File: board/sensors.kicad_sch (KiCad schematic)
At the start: 59 parts, among them J2 SWIM, U6 STM8S003F3P, U7 MAX-M8C, U8 LM324, U9 LM324

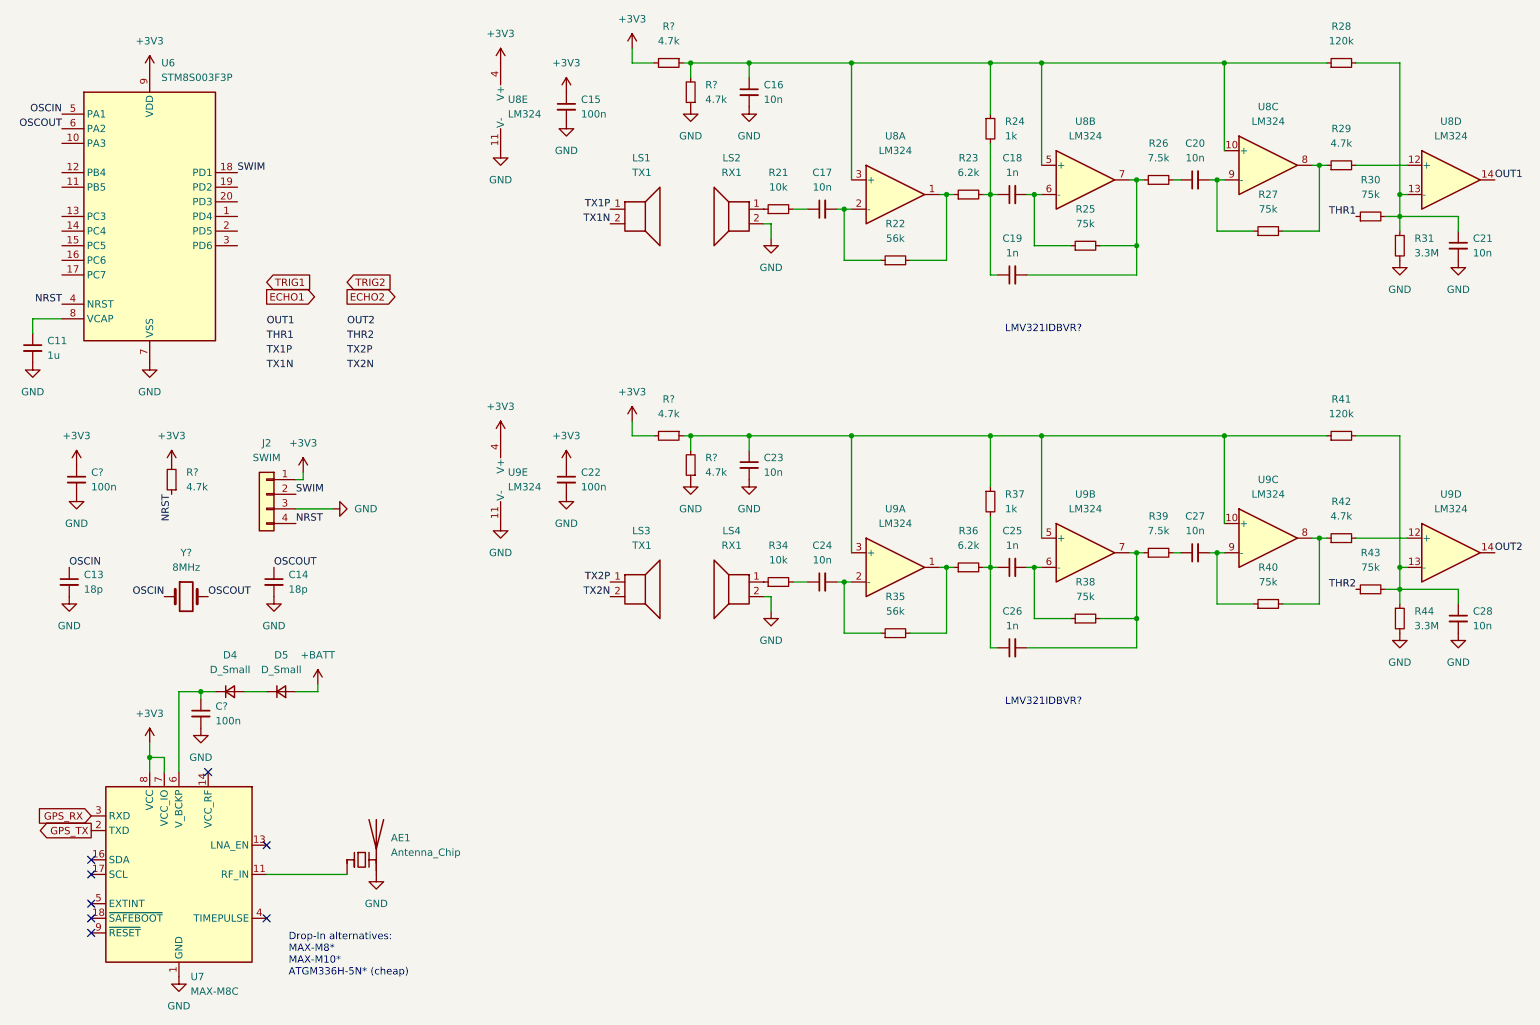
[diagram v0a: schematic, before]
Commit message: New power management IC, some cleanup
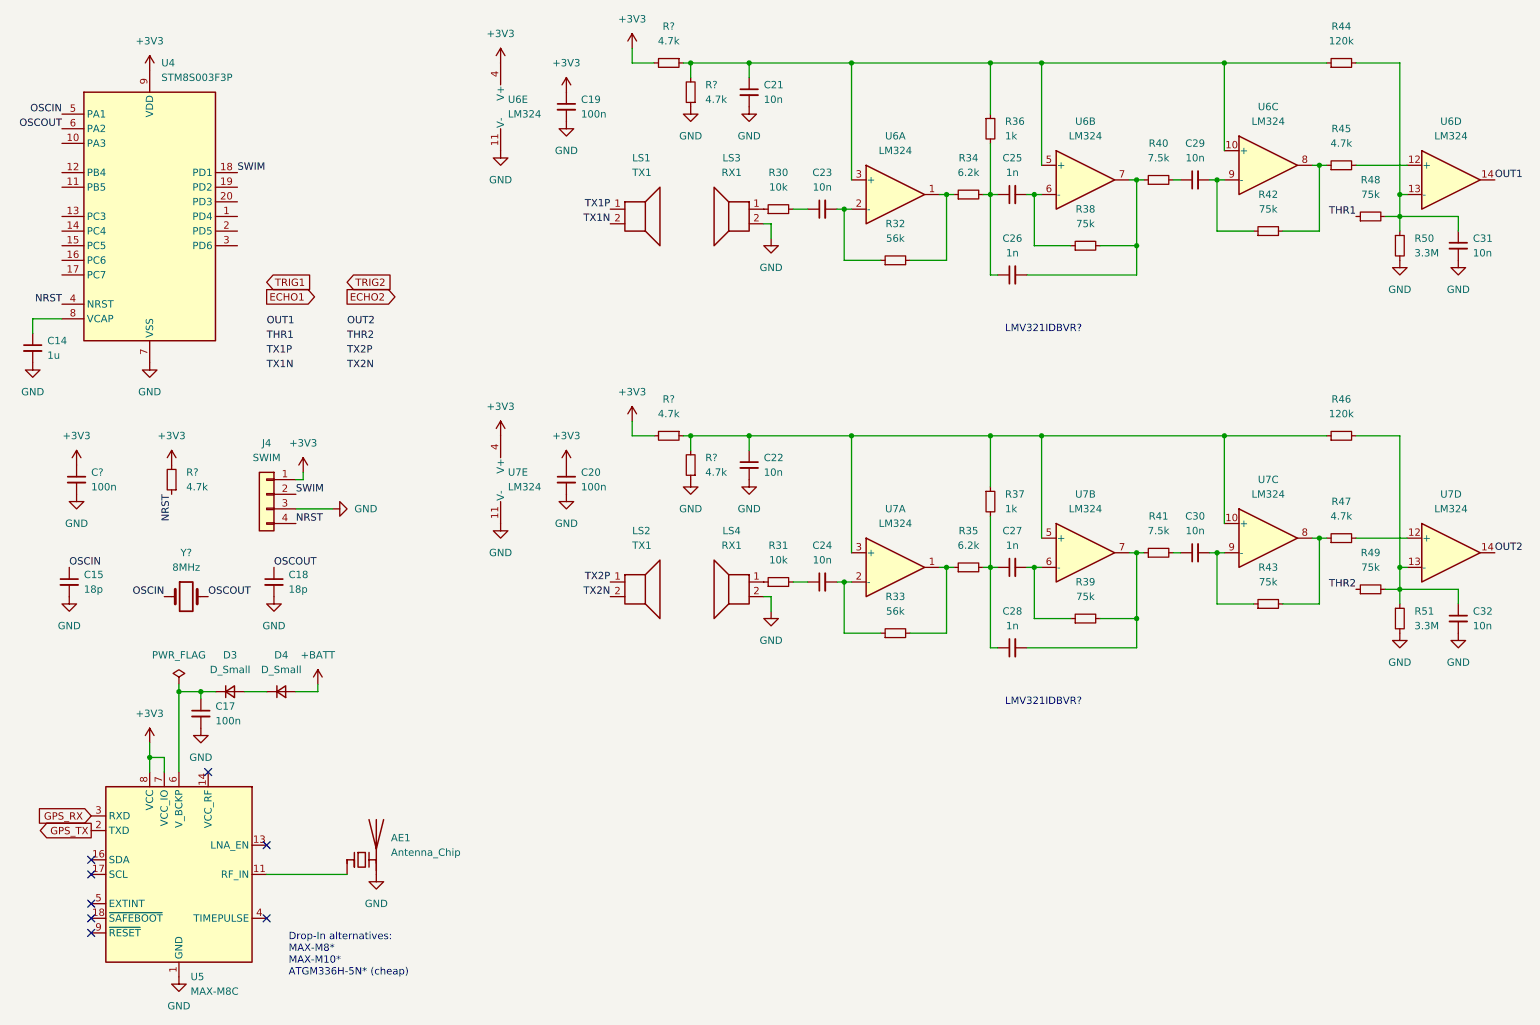
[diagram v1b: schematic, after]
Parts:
- gave numbers to parts that had none: 1
- renumbered C11 to C14, C13 to C15, C14 to C18, C15 to C19, C22 to C20, C16 to C21, C23 to C22, C17 to C23, C18 to C25, C19 to C26, C25 to C27, C26 to C28, C20 to C29, C27 to C30, C21 to C31, C28 to C32, D4 to D3, D5 to D4, J2 to J4, LS3 to LS2, LS2 to LS3, R21 to R30, R34 to R31, R22 to R32, R35 to R33, R23 to R34, R36 to R35, R24 to R36, R25 to R38, R38 to R39, R26 to R40, R39 to R41, R27 to R42, R40 to R43, R28 to R44, R29 to R45, R41 to R46, R42 to R47, R30 to R48, R43 to R49, R31 to R50, R44 to R51, U6 to U4, U7 to U5, U8 to U6, U9 to U7

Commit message: Add kibot/kicost config and sample cost entry for antenna chip
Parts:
- AE1: kicost:JLC:pricing (none) -> 1:USD1.0297; 10:USD0.9651; 100:USD0.5724; 1000:USD0.6065
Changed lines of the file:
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@@
+      (effects (font (size 1.27 1.27)) hide)
+    )
+    (property "kicost:JLC:pricing" "1:USD1.0297; 10:USD0.9651; 100:USD0.5724; 1000:USD0.6065" (id 13) (at 76.2 168.91 0)
       (effects (font (size 1.27 1.27)) hide)
     )

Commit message: Add kibot:JLC:pricing from existing columns
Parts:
- AE1: kicost:JLC:pricing 1:USD1.0297; 10:USD0.9651; 100:USD0.5724; 1000:USD0.6065 -> 1: USD 1.0297; 10: USD 0.8651; 100: USD 0.5724; 1000: USD0.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
- C14: kicost:JLC:pricing (none) -> 1: USD 0.056; 10: USD 0.0056; 100: USD 0.0028; 1000: USD0.0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
- C17, C19, C20, C?: kicost:JLC:pricing (none) -> 1: USD 0.042; 10: USD 0.0042; 100: USD 0.0021; 1000: USD0.0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
- J4: kicost:JLC:pricing (none) -> 1: USD 0.1105; 10: USD 0.0442; 100: USD 0.0179; 1000: USD0.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
- LS1, LS2, LS3, LS4: kicost:JLC:pricing (none) -> 1: USD 1.5383; 10: USD 1.2985; 100: USD 1.1671; 1000: USD1.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
- U4: kicost:JLC:pricing (none) -> 1: USD 0.7209; 10: USD 0.7084; 100: USD 0.7084; 1000: USD0.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
- U5: kicost:JLC:pricing (none) -> 1: USD 21; 10: USD 15.73; 100: USD 10.32; 1000: USD10.32
- U6, U7: kicost:JLC:pricing (none) -> 1: USD 0.1235; 10: USD 0.0971; 100: USD 0.0728; 1000: USD0.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
- Y?: kicost:JLC:pricing (none) -> 1: USD 0.164; 10: USD 0.082; 100: USD 0.0576; 1000: USD0.04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
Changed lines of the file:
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@@
+      (effects (font (size 1.27 1.27)) hide)
+    )
+    (property "kicost:JLC:pricing" "1: USD 0.042; 10: USD 0.0042; 100: USD 0.0021; 1000: USD0.0014" (id 16) (at 26.67 102.87 0)
       (effects (font (size 1.27 1.27)) hide)
     )
@@
       (effects (font (size 1.27 1.27)) hide)
     )
-    (property "kicost:JLC:pricing" "1:USD1.0297; 10:USD0.9651; 100:USD0.5724; 1000:USD0.6065" (id 13) (at 76.2 168.91 0)
+    (property "kicost:JLC:pricing" "1: USD 1.0297; 10: USD 0.8651; 100: USD 0.5724; 1000: USD0.6065" (id 13) (at 76.2 168.91 0)
       (effects (font (size 1.27 1.27)) hide)
     )
@@
       (effects (font (size 1.27 1.27)) hide)
     )
+    (property "kicost:JLC:pricing" "1: USD 1.5383; 10: USD 1.2985; 100: USD 1.1671; 1000: USD1.0179" (id 13) (at 124.46 55.88 0)
+      (effects (font (size 1.27 1.27)) hide)
+    )
     (pin "1")
     (pin "2")
@@
     )
     (property "PCBA" "no" (id 11) (at 44.45 171.45 0)
+      (effects (font (size 1.27 1.27)) hide)
+    )
+    (property "kicost:JLC:pricing" "1: USD 21; 10: USD 15.73; 100: USD 10.32; 1000: USD10.32" (id 12) (at 44.45 171.45 0)
       (effects (font (size 1.27 1.27)) hide)
     )
@@
       (effects (font (size 1.27 1.27)) hide)
     )
+    (property "kicost:JLC:pricing" "1: USD 1.5383; 10: USD 1.2985; 100: USD 1.1671; 1000: USD1.0179" (id 13) (at 140.97 55.88 0)
+      (effects (font (size 1.27 1.27)) hide)
+    )
     (pin "1")
     (pin "2")
@@
     )
     (property "PCBA" "yes" (id 12) (at 265.43 50.8 0)
+      (effects (font (size 1.27 1.27)) hide)
+    )
+    (property "kicost:JLC:pricing" "1: USD 0.1235; 10: USD 0.0971; 100: USD 0.0728; 1000: USD0.0696" (id 13) (at 265.43 50.8 0)
       (effects (font (size 1.27 1.27)) hide)
     )
@@
       (effects (font (size 1.27 1.27)) hide)
     )
+    (property "kicost:JLC:pricing" "1: USD 0.1235; 10: USD 0.0971; 100: USD 0.0728; 1000: USD0.0696" (id 13) (at 102.87 38.1 0)
+      (effects (font (size 1.27 1.27)) hide)
+    )
     (pin "1")
     (pin "2")
@@
       (effects (font (size 1.27 1.27)) hide)
     )
+    (property "kicost:JLC:pricing" "1: USD 0.042; 10: USD 0.0042; 100: USD 0.0021; 1000: USD0.0014" (id 13) (at 111.76 38.1 0)
+      (effects (font (size 1.27 1.27)) hide)
+    )
     (pin "1")
     (pin "2")
@@
     )
     (property "PCBA" "yes" (id 12) (at 102.87 102.87 0)
+      (effects (font (size 1.27 1.27)) hide)
+    )
+    (property "kicost:JLC:pricing" "1: USD 0.1235; 10: USD 0.0971; 100: USD 0.0728; 1000: USD0.0696" (id 13) (at 102.87 102.87 0)
       (effects (font (size 1.27 1.27)) hide)
     )
@@
       (effects (font (size 1.27 1.27)) hide)
     )
+    (property "kicost:JLC:pricing" "1: USD 0.056; 10: USD 0.0056; 100: USD 0.0028; 1000: USD0.0027" (id 13) (at 19.05 80.01 0)
+      (effects (font (size 1.27 1.27)) hide)
+    )
     (pin "1")
     (pin "2")
@@
     )
     (property "PCBA" "yes" (id 12) (at 233.68 113.03 0)
+      (effects (font (size 1.27 1.27)) hide)
+    )
+    (property "kicost:JLC:pricing" "1: USD 0.1235; 10: USD 0.0971; 100: USD 0.0728; 1000: USD0.0696" (id 13) (at 233.68 113.03 0)
       (effects (font (size 1.27 1.27)) hide)
     )
@@
       (effects (font (size 1.27 1.27)) hide)
     )
+    (property "kicost:JLC:pricing" "1: USD 1.5383; 10: USD 1.2985; 100: USD 1.1671; 1000: USD1.0179" (id 13) (at 140.97 120.65 0)
+      (effects (font (size 1.27 1.27)) hide)
+    )
     (pin "1")
     (pin "2")
@@
     )
     (property "PCBA" "yes" (id 12) (at 201.93 50.8 0)
+      (effects (font (size 1.27 1.27)) hide)
+    )
+    (property "kicost:JLC:pricing" "1: USD 0.1235; 10: USD 0.0971; 100: USD 0.0728; 1000: USD0.0696" (id 13) (at 201.93 50.8 0)
       (effects (font (size 1.27 1.27)) hide)
     )
@@
       (effects (font (size 1.27 1.27)) hide)
     )
+    (property "kicost:JLC:pricing" "1: USD 0.042; 10: USD 0.0042; 100: USD 0.0021; 1000: USD0.0014" (id 13) (at 48.26 143.51 0)
+      (effects (font (size 1.27 1.27)) hide)
+    )
     (pin "1")
     (pin "2")
@@
       (effects (font (size 1.27 1.27)) hide)
     )
+    (property "kicost:JLC:pricing" "1: USD 0.042; 10: USD 0.0042; 100: USD 0.0021; 1000: USD0.0014" (id 13) (at 111.76 102.87 0)
+      (effects (font (size 1.27 1.27)) hide)
+    )
     (pin "1")
     (pin "2")
@@
     )
     (property "PCBA" "yes" (id 12) (at 233.68 48.26 0)
+      (effects (font (size 1.27 1.27)) hide)
+    )
+    (property "kicost:JLC:pricing" "1: USD 0.1235; 10: USD 0.0971; 100: USD 0.0728; 1000: USD0.0696" (id 13) (at 233.68 48.26 0)
       (effects (font (size 1.27 1.27)) hide)
     )
@@
       (effects (font (size 1.27 1.27)) hide)
     )
+    (property "kicost:JLC:pricing" "1: USD 0.1105; 10: USD 0.0442; 100: USD 0.0179; 1000: USD0.0142" (id 13) (at 59.69 105.41 0)
+      (effects (font (size 1.27 1.27)) hide)
+    )
     (pin "1")
     (pin "2")
@@
     )
     (property "PCBA" "yes" (id 12) (at 39.37 57.15 0)
+      (effects (font (size 1.27 1.27)) hide)
+    )
+    (property "kicost:JLC:pricing" "1: USD 0.7209; 10: USD 0.7084; 100: USD 0.7084; 1000: USD0.7084" (id 13) (at 39.37 57.15 0)
       (effects (font (size 1.27 1.27)) hide)
     )
@@
     )
     (property "PCBA" "yes" (id 12) (at 168.91 118.11 0)
+      (effects (font (size 1.27 1.27)) hide)
+    )
+    (property "kicost:JLC:pricing" "1: USD 0.1235; 10: USD 0.0971; 100: USD 0.0728; 1000: USD0.0696" (id 13) (at 168.91 118.11 0)
       (effects (font (size 1.27 1.27)) hide)
     )
@@
       (effects (font (size 1.27 1.27)) hide)
     )
+    (property "kicost:JLC:pricing" "1: USD 0.1235; 10: USD 0.0971; 100: USD 0.0728; 1000: USD0.0696" (id 13) (at 201.93 115.57 0)
+      (effects (font (size 1.27 1.27)) hide)
+    )
     (pin "1")
     (pin "2")
@@
       (effects (font (size 1.27 1.27)) hide)
     )
+    (property "kicost:JLC:pricing" "1: USD 0.1235; 10: USD 0.0971; 100: USD 0.0728; 1000: USD0.0696" (id 13) (at 265.43 115.57 0)
+      (effects (font (size 1.27 1.27)) hide)
+    )
     (pin "1")
     (pin "2")
@@
       (effects (font (size 1.27 1.27)) hide)
     )
+    (property "kicost:JLC:pricing" "1: USD 0.1235; 10: USD 0.0971; 100: USD 0.0728; 1000: USD0.0696" (id 13) (at 168.91 53.34 0)
+      (effects (font (size 1.27 1.27)) hide)
+    )
     (pin "1")
     (pin "2")
@@
       (effects (font (size 1.27 1.27)) hide)
     )
+    (property "kicost:JLC:pricing" "1: USD 1.5383; 10: USD 1.2985; 100: USD 1.1671; 1000: USD1.0179" (id 13) (at 124.46 120.65 0)
+      (effects (font (size 1.27 1.27)) hide)
+    )
     (pin "1")
     (pin "2")
@@
       (effects (font (size 1.27 1.27)) hide)
     )
+    (property "kicost:JLC:pricing" "1: USD 0.164; 10: USD 0.082; 100: USD 0.0576; 1000: USD0.0464" (id 16) (at 45.72 123.19 0)
+      (effects (font (size 1.27 1.27)) hide)
+    )

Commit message: Add more footprints, prices and part numbers
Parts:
- C14: footprint (none) -> Capacitor_SMD:C_0603_1608Metric; kicost:JLC:pricing 1: USD 0.056; 10: USD 0.0056; 100: USD 0.0028; 1000: USD0.0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 -> 1: USD 0.056; 10: USD 0.0056; 100: USD 0.0028; 1000: USD 0.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
- C15, C18: footprint (none) -> Capacitor_SMD:C_0603_1608Metric; JLC_BasicPart (none) -> yes; JLC_PN (none) -> C1647; MPN (none) -> CL10C180JB8NNNC; Manufacturer (none) -> Samsung Electro-Mechanics; kicost:JLC:pricing (none) -> 1: USD 0.0069; 200: USD 0.0058; 800: USD 0.0051; 1600: USD 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
- C17, C19, C20, C?: footprint (none) -> Capacitor_SMD:C_0603_1608Metric; kicost:JLC:pricing 1: USD 0.042; 10: USD 0.0042; 100: USD 0.0021; 1000: USD0.0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 -> 1: USD 0.0020; 200: USD 0.0016; 800: USD 0.0013; 1600: USD 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
- C21, C22, C23, C24, C29, C30, C31, C32: footprint (none) -> Capacitor_SMD:C_0603_1608Metric; JLC_BasicPart (none) -> yes; JLC_PN (none) -> C57112; MPN (none) -> 0603B103K500NT; Manufacturer (none) -> FH (Guangdong Fenghua Advanced Tech); kicost:JLC:pricing (none) -> 1: USD 0.0012
- C25, C26, C27, C28: footprint (none) -> Capacitor_SMD:C_0603_1608Metric; JLC_BasicPart (none) -> yes; JLC_PN (none) -> C1588; MPN (none) -> CL10B102KB8NNNC; Manufacturer (none) -> Samsung Electro-Mechanics; kicost:JLC:pricing (none) -> 1: USD 0.0026; 200: USD 0.0020; 800: USD 0.0017; 1600: USD 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
- D3, D4: footprint (none) -> Diode_SMD:D_SMA; JLC_BasicPart (none) -> yes; JLC_PN (none) -> C2480; MPN (none) -> SS14; Manufacturer (none) -> MDD（Microdiode Electronics）; kicost:JLC:pricing (none) -> 1: USD 0.0137; 50: USD 0.0111; 150: USD 0.0097; 500: USD 0.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
- J4: kicost:JLC:pricing 1: USD 0.1105; 10: USD 0.0442; 100: USD 0.0179; 1000: USD0.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 -> 1: USD 0.1105; 10: USD 0.0442; 100: USD 0.0179; 1000: USD 0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
- LS1, LS2, LS3, LS4: kicost:JLC:pricing 1: USD 1.5383; 10: USD 1.2985; 100: USD 1.1671; 1000: USD1.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 -> 1: USD 1.5383; 10: USD 1.2985; 100: USD 1.1671; 1000: USD 1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
- R30, R31: footprint (none) -> Resistor_SMD:R_0603_1608Metric; JLC_BasicPart (none) -> yes; JLC_PN (none) -> C25197; MPN (none) -> 0603WAF510KT5E; Manufacturer (none) -> UNI-ROYAL(Uniroyal Elec); kicost:JLC:pricing (none) -> 1: USD 0.0014; 200: USD 0.0011; 1000: USD 0.0009; 2000: USD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
- R32, R33: footprint (none) -> Resistor_SMD:R_0603_1608Metric; JLC_BasicPart (none) -> yes; JLC_PN (none) -> C23206; MPN (none) -> 0603WAF5602T5E; Manufacturer (none) -> UNI-ROYAL(Uniroyal Elec); kicost:JLC:pricing (none) -> 1: USD 0.0009; 200: USD 0.0007; 1000: USD 0.0006; 2000: USD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
- R34, R35: footprint (none) -> Resistor_SMD:R_0603_1608Metric; JLC_BasicPart (none) -> yes; JLC_PN (none) -> C4260; MPN (none) -> 0603WAF6201T5E; Manufacturer (none) -> UNI-ROYAL(Uniroyal Elec); kicost:JLC:pricing (none) -> 1: USD 0.0009; 200: USD 0.0007; 1000: USD 0.0006; 10000: US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
- R36, R37: footprint (none) -> Resistor_SMD:R_0603_1608Metric; JLC_BasicPart (none) -> yes; JLC_PN (none) -> C21190; MPN (none) -> 0603WAF1001T5E; Manufacturer (none) -> UNI-ROYAL(Uniroyal Elec); kicost:JLC:pricing (none) -> 1: USD 0.0005; 200: USD 0.0004
- R38, R39, R42, R43, R48, R49: footprint (none) -> Resistor_SMD:R_0603_1608Metric; JLC_BasicPart (none) -> yes; JLC_PN (none) -> C23242; MPN (none) -> 0603WAF7502T5E; Manufacturer (none) -> UNI-ROYAL(Uniroyal Elec); kicost:JLC:pricing (none) -> 1: USD 0.0010; 200: USD 0.0007; 1000: USD 0.0006; 10000: US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
- R40, R41: footprint (none) -> Resistor_SMD:R_0603_1608Metric; JLC_BasicPart (none) -> yes; JLC_PN (none) -> C23234; MPN (none) -> 0603WAF7501T5E; Manufacturer (none) -> UNI-ROYAL(Uniroyal Elec); kicost:JLC:pricing (none) -> 1: USD 0.0009; 200: USD 0.0007; 1000: USD 0.0006; 10000: US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
- R44, R46: footprint (none) -> Resistor_SMD:R_0603_1608Metric; JLC_BasicPart (none) -> yes; JLC_PN (none) -> C25808; MPN (none) -> 0603WAF1203T5E; Manufacturer (none) -> UNI-ROYAL(Uniroyal Elec); kicost:JLC:pricing (none) -> 1: USD 0.0010; 200: USD 0.0007; 1000: USD 0.0006; 10000: US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
- R45, R47, R? (x5): footprint (none) -> Resistor_SMD:R_0603_1608Metric; JLC_BasicPart (none) -> yes; JLC_PN (none) -> C23162; MPN (none) -> 0603WAF4701T5E; Manufacturer (none) -> UNI-ROYAL(Uniroyal Elec); kicost:JLC:pricing (none) -> 1: USD 0.0009; 200: USD 0.0007; 1000: USD 0.0006; 2000: USD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
- R50, R51: footprint (none) -> Resistor_SMD:R_0603_1608Metric; JLC_BasicPart (none) -> no; JLC_PN (none) -> C39227; MPN (none) -> 0603WAJ0335T5E; Manufacturer (none) -> UNI-ROYAL(Uniroyal Elec); kicost:JLC:pricing (none) -> 1: USD 0.0009; 200: USD 0.0007; 1000: USD 0.0006; 2000: USD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
- U4: kicost:JLC:pricing 1: USD 0.7209; 10: USD 0.7084; 100: USD 0.7084; 1000: USD0.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 -> 1: USD 0.7209; 10: USD 0.7084; 100: USD 0.7084; 1000: USD 0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
- U5: kicost:JLC:pricing 1: USD 21; 10: USD 15.73; 100: USD 10.32; 1000: USD10.32 -> 1: USD 21; 10: USD 15.73; 100: USD 10.32; 1000: USD 10.32
- U6, U7: footprint (none) -> Package_SO:SOIC-14_3.9x8.7mm_P1.27mm
